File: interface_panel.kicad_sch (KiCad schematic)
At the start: 20 parts, among them J1 Conn_02x04_Odd_Even, J2 but1, J3 but2, J4 but3, J5 Led, U2 ATmega328P-P, Y1 Crystal

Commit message: oled Production
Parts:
- removed J1: Conn_02x04_Odd_Even, Connector_IDC:IDC-Header_2x04_P2.54mm_Vertical, symbol Connector_Generic:Conn_02x04_Odd_Even
- added J6: Conn_01x02_Socket, Connector_PinHeader_1.27mm:PinHeader_1x02_P1.27mm_Vertical, symbol Connector:Conn_01x02_Socket
- added J7: Conn_02x05_Odd_Even, Connector_IDC:IDC-Header_2x05_P2.54mm_Vertical, symbol Connector_Generic:Conn_02x05_Odd_Even
- added R2: 10k, Resistor_THT:R_Axial_DIN0204_L3.6mm_D1.6mm_P5.08mm_Horizontal, symbol Device:R
- H1, H2, H3, H4: footprint (none) -> MountingHole:MountingHole_2.2mm_M2
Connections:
- net 5V: now also U2.20 (AVCC), J7.1 (Pin_1), R2.1
- net BT-1: now also J7.5 (Pin_5)
- net BT-2: now also J7.7 (Pin_7)
- net BT-Pwr: now also J7.3 (Pin_3)
- net GND: now also J6.2 (Pin_2), J7.2 (Pin_2)
- net RX: now also J7.6 (Pin_6)
- net S. LED: now also J7.4 (Pin_4)
- net TX: now also J7.8 (Pin_8)
- net at U2.1 (~{RESET}/PC6): now also J6.1 (Pin_1), R2.2
- net D7: now reaches U2.13 (PD7)
- net D7: now also J7.10 (Pin_10)
- net D11: now reaches U2.17 (PB3)
- net D11: now also J7.9 (Pin_9)

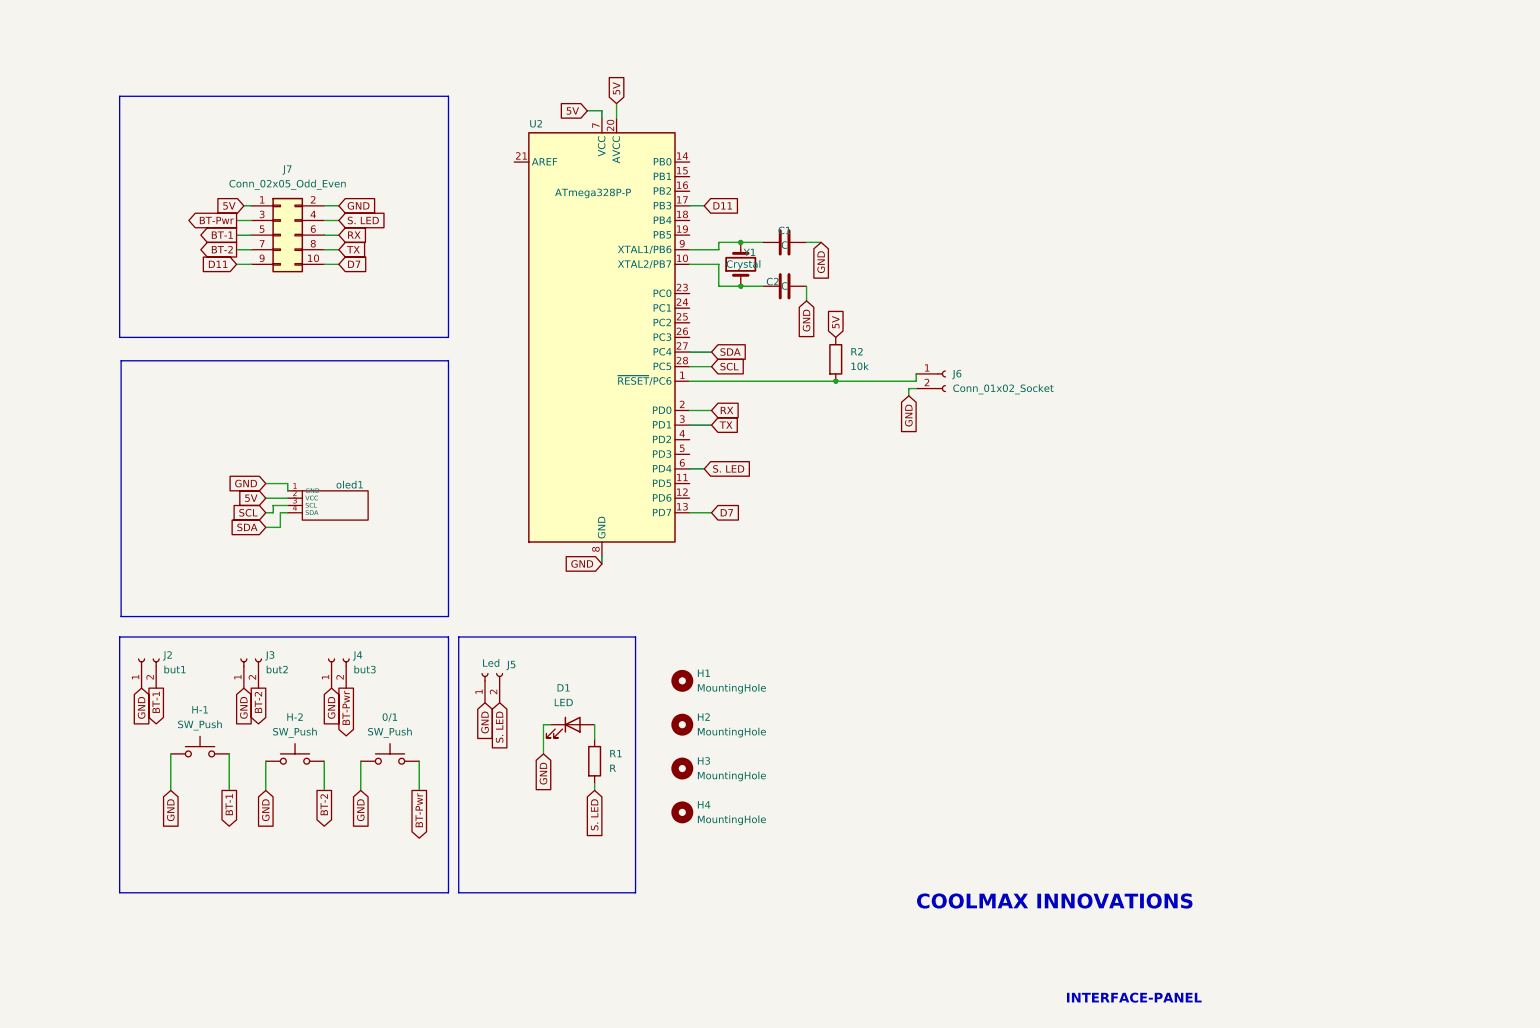
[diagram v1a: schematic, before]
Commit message: 7segment added
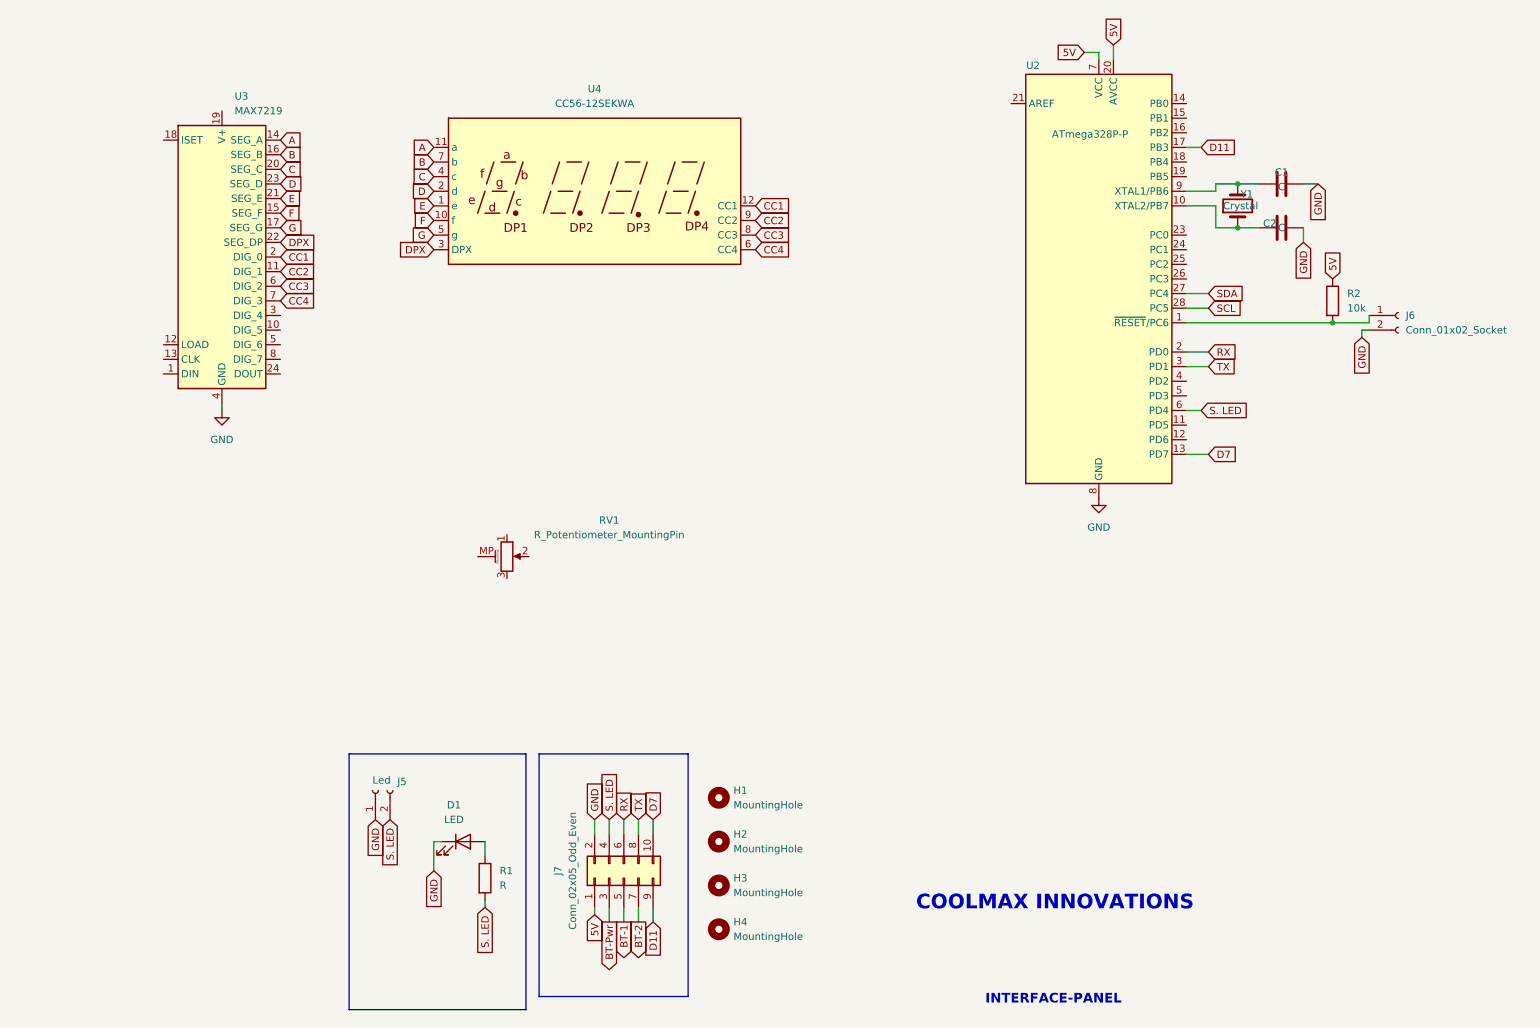
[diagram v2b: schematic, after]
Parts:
- removed 0/1, H-1, H-2: SW_Push, pushbutt_12x12x7.3:SW_TS14-1212-140-BK-160-SCR-D, symbol Switch:SW_Push
- removed J2: but1, Connector_JST:JST_EH_B2B-EH-A_1x02_P2.50mm_Vertical, symbol Connector:Conn_01x02_Socket
- removed J3: but2, Connector_JST:JST_EH_B2B-EH-A_1x02_P2.50mm_Vertical, symbol Connector:Conn_01x02_Socket
- removed J4: but3, Connector_JST:JST_EH_B2B-EH-A_1x02_P2.50mm_Vertical, symbol Connector:Conn_01x02_Socket
- removed U1: ~, symbol New_Library:oled128x32
- removed oled1: ~, oled0.9in:MODULE_DM-OLED096-636, symbol New_Library:oled
- added RV1: R_Potentiometer_MountingPin, Potentiometer_THT:Potentiometer_Alps_RK09K_Single_Horizontal, symbol Device:R_Potentiometer_MountingPin
- added U3: MAX7219, Package_DIP:DIP-24_W7.62mm, symbol Driver_LED:MAX7219
- added U4: CC56-12SEKWA, Display_7Segment:CA56-12SEKWA, symbol Display_Character:CC56-12SEKWA
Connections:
- net GND: now also U3.4 (GND), U3.9 (GND)
- new net A: U3.14 (SEG_A), U4.11 (a)
- new net B: U3.16 (SEG_B), U4.7 (b)
- new net C: U3.20 (SEG_C), U4.4 (c)
- new net CC1: U3.2 (DIG_0), U4.12 (CC1)
- new net CC2: U3.11 (DIG_1), U4.9 (CC2)
- new net CC3: U3.6 (DIG_2), U4.8 (CC3)
- new net CC4: U3.7 (DIG_3), U4.6 (CC4)
- new net D: U3.23 (SEG_D), U4.2 (d)
- new net DPX: U3.22 (SEG_DP), U4.3 (DPX)
- new net E: U3.21 (SEG_E), U4.1 (e)
- new net F: U3.15 (SEG_F), U4.10 (f)
- new net G: U3.17 (SEG_G), U4.5 (g)
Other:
- moved on the sheet: C1, C2, D1, H1, H2, H3, H4, J5, J6, J7, R1, R2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

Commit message: Segment-added
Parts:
- removed RV1: R_Potentiometer_MountingPin, Potentiometer_THT:Potentiometer_Alps_RK09K_Single_Horizontal, symbol Device:R_Potentiometer_MountingPin
- removed U3: MAX7219, Package_DIP:DIP-24_W7.62mm, symbol Driver_LED:MAX7219
- removed U4: CC56-12SEKWA, Display_7Segment:CA56-12SEKWA, symbol Display_Character:CC56-12SEKWA
- added H5, H6, PWR1: SW_Push, Button_Switch_THT:SW_PUSH-12mm, symbol Switch:SW_Push
- added Q1, Q2: BC547, Package_TO_SOT_THT:TO-92_Inline, symbol Transistor_BJT:BC547
- added R10, R11, R12, R3, R4, R5, R6, R7, R8, R9: R, Resistor_THT:R_Axial_DIN0204_L3.6mm_D1.6mm_P5.08mm_Horizontal, symbol Device:R
- added U1, U4: SM420561N, Display_7Segment:7SegmentLED_LTS6760_LTS6780, symbol Display_Character:SM420561N
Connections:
- net A: now also R7.2, U1.7 (A), U4.7 (A)
- net B: now also R8.2, U1.6 (B), U4.6 (B)
- net BT-1: now also H5.1
- net BT-2: now also H6.1
- net BT-Pwr: now also PWR1.1
- net C: now also R9.2, U1.4 (C), U4.4 (C)
- net CC1: now also Q1.2 (B), R3.2
- net CC2: now also Q2.2 (B), R4.2
- net D: now also R10.2, U1.2 (D), U4.2 (D)
- net D7: no longer U2.13 (PD7)
- net DPX: now also R6.2, U1.5 (DP), U4.5 (DP)
- net E: now also R11.2, U1.1 (E), U4.1 (E)
- net F: now also R12.2, U1.9 (F), U4.9 (F)
- net G: now also R5.2, U1.10 (G), U4.10 (G)
- net GND: now also H5.2, H6.2, PWR1.2, Q1.3 (E), Q2.3 (E)
- net S. LED: now also U2.18 (PB4); no longer U2.6 (PD4)
- net at U2.11 (PD5): now also R9.1
- net at U2.12 (PD6): now also R10.1
- net at U2.14 (PB0): now also R12.1
- net at U2.15 (PB1): now also R5.1
- net at U2.16 (PB2): now also R3.1
- net D13: now reaches U2.19 (PB5)
- net D13: now also J7.9 (Pin_9)
- net at U2.4 (PD2): now also R6.1
- net at U2.5 (PD3): now also R7.1
- net D11: no longer names the net of U2.17 (PB3)
- net D11: now also R4.1; no longer J7.9 (Pin_9)
- net SCL: no longer names the net of U2.28 (PC5)
- net SDA: no longer names the net of U2.27 (PC4)
- new net: Q2.1 (C), U4.3 (CC), U4.8 (CC)
- new net: Q1.1 (C), U1.3 (CC), U1.8 (CC)
- new net: R11.1, U2.13 (PD7)
- new net: R8.1, U2.6 (PD4)

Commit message: updated
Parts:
- added J1: B1, Connector_JST:JST_EH_B2B-EH-A_1x02_P2.50mm_Vertical, symbol Connector:Conn_01x02_Socket
- added J2: B2, Connector_JST:JST_EH_B2B-EH-A_1x02_P2.50mm_Vertical, symbol Connector:Conn_01x02_Socket
- added J3: BP, Connector_JST:JST_EH_B2B-EH-A_1x02_P2.50mm_Vertical, symbol Connector:Conn_01x02_Socket
- added JP1: sda, Jumper:SolderJumper-2_P1.3mm_Open_Pad1.0x1.5mm, symbol Jumper:SolderJumper_2_Open
- added JP2: scl, Jumper:SolderJumper-2_P1.3mm_Open_Pad1.0x1.5mm, symbol Jumper:SolderJumper_2_Open
- added R13, R14: R, Resistor_THT:R_Axial_DIN0204_L3.6mm_D1.6mm_P5.08mm_Horizontal, symbol Device:R
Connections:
- net BT-1: now also J1.2 (Pin_2)
- net BT-2: now also J2.2 (Pin_2)
- net BT-Pwr: now also J3.2 (Pin_2)
- net CC1: now also R13.2
- net CC2: now also R14.2
- net GND: now also J1.1 (Pin_1), J2.1 (Pin_1), J3.1 (Pin_1), R13.1, R14.1
- net RX: now also JP1.2 (B)
- net TX: now also JP2.2 (B)
- net at U2.27 (PC4): now also JP1.1 (A)
- net at U2.28 (PC5): now also JP2.1 (A)
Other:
- moved on the sheet: R2

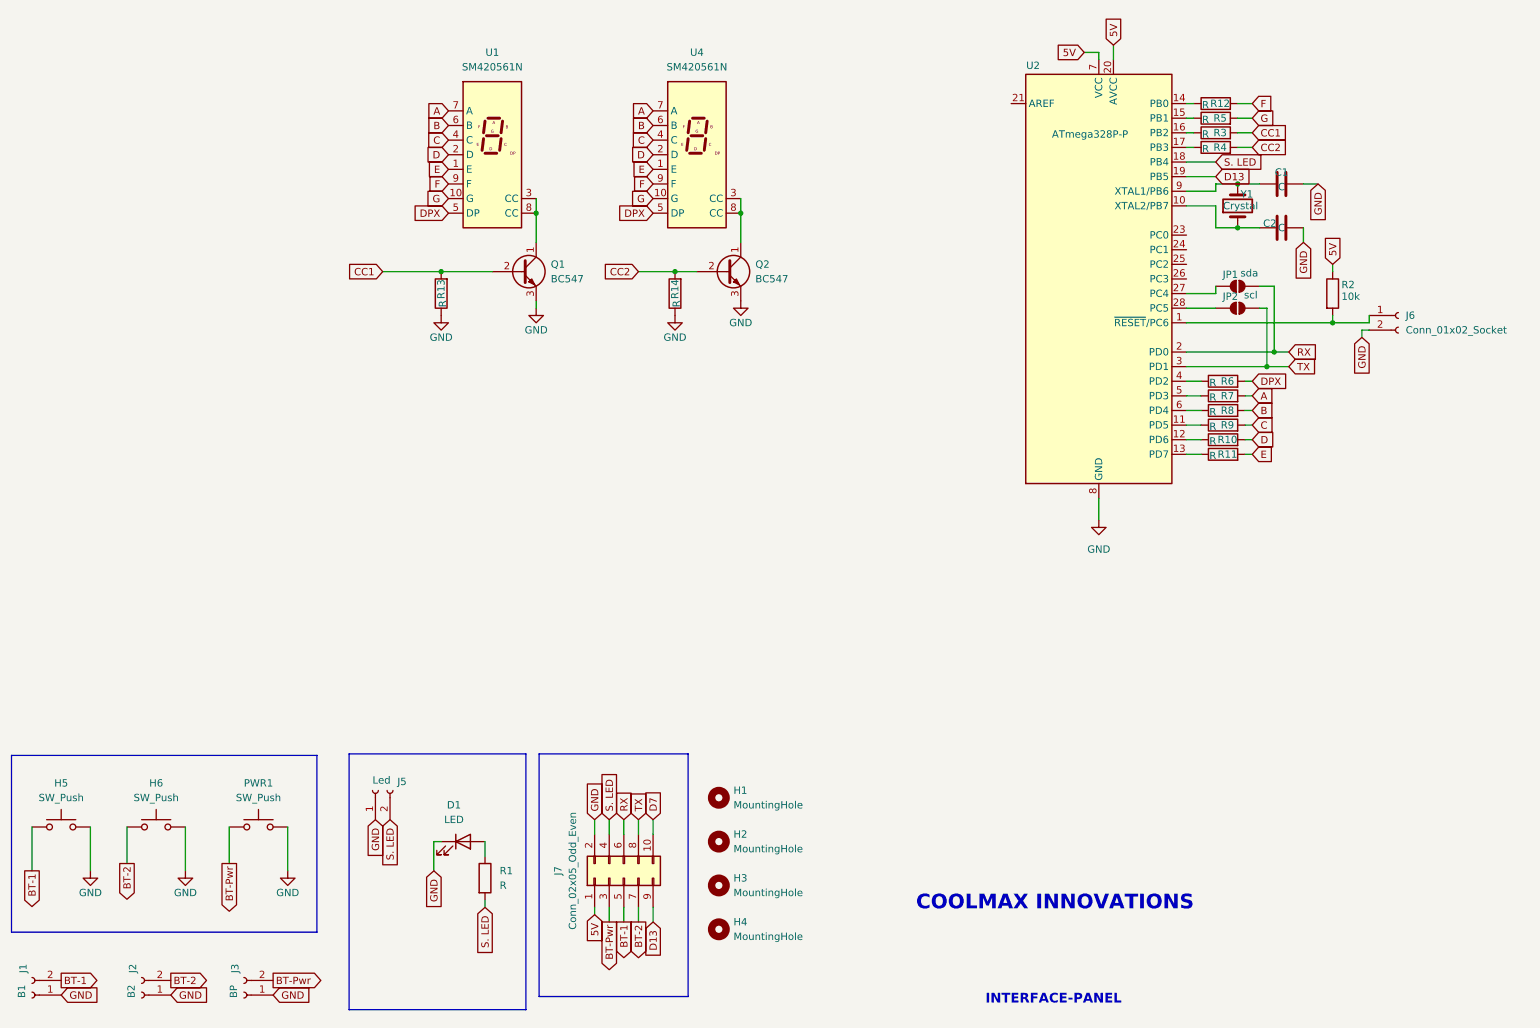
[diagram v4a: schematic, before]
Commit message: new-layout with 7seg and fpc connector
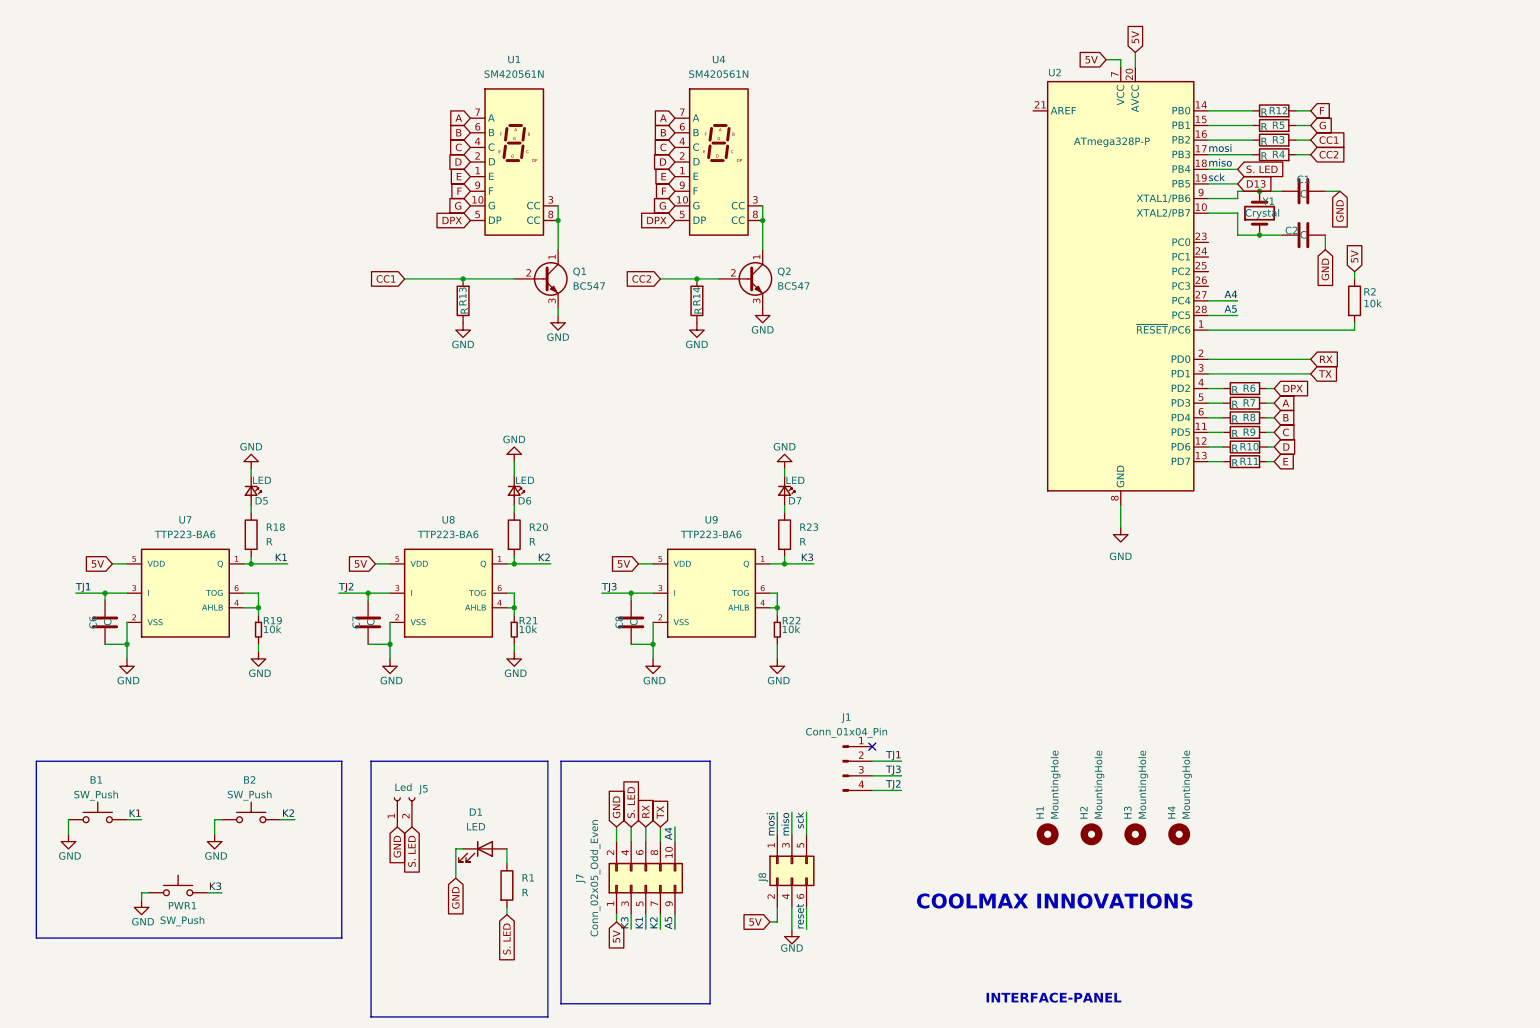
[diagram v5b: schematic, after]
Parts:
- removed H5, H6: SW_Push, Button_Switch_THT:SW_PUSH-12mm, symbol Switch:SW_Push
- removed J1: B1, Connector_JST:JST_EH_B2B-EH-A_1x02_P2.50mm_Vertical, symbol Connector:Conn_01x02_Socket
- removed J2: B2, Connector_JST:JST_EH_B2B-EH-A_1x02_P2.50mm_Vertical, symbol Connector:Conn_01x02_Socket
- removed J3: BP, Connector_JST:JST_EH_B2B-EH-A_1x02_P2.50mm_Vertical, symbol Connector:Conn_01x02_Socket
- removed J6: Conn_01x02_Socket, Connector_PinHeader_1.27mm:PinHeader_1x02_P1.27mm_Vertical, symbol Connector:Conn_01x02_Socket
- removed JP1: sda, Jumper:SolderJumper-2_P1.3mm_Open_Pad1.0x1.5mm, symbol Jumper:SolderJumper_2_Open
- removed JP2: scl, Jumper:SolderJumper-2_P1.3mm_Open_Pad1.0x1.5mm, symbol Jumper:SolderJumper_2_Open
- added B1, B2: SW_Push, Button_Switch_THT:SW_PUSH-12mm, symbol Switch:SW_Push
- added C6, C7, C8: C, Capacitor_SMD:C_1206_3216Metric_Pad1.33x1.80mm_HandSolder, symbol Device:C
- added D5, D6, D7: LED, PCM_SparkFun-LED:LED_1206_3216Metric, symbol PCM_SparkFun-LED:LED
- added J1: Conn_01x04_Pin, Connector_FFC-FPC:Amphenol_F32Q-1A7x1-11004_1x04-1MP_P0.5mm_Horizontal, symbol Connector:Conn_01x04_Pin
- added J8: `, Connector_PinHeader_2.54mm:PinHeader_2x03_P2.54mm_Vertical, symbol Connector_Generic:Conn_02x03_Odd_Even
- added R18, R20, R23: R, Resistor_SMD:R_1206_3216Metric_Pad1.30x1.75mm_HandSolder, symbol Device:R
- added R19, R21, R22: 10k, Resistor_SMD:R_1206_3216Metric_Pad1.30x1.75mm_HandSolder, symbol Device:R
- added U7, U8, U9: TTP223-BA6, TTP223-BA6:SOT23-6, symbol TTP223:TTP223-BA6
- C1, C2: footprint Capacitor_THT:C_Disc_D3.0mm_W1.6mm_P2.50mm -> Capacitor_SMD:C_1206_3216Metric_Pad1.33x1.80mm_HandSolder
- D1: footprint LED_THT:LED_D3.0mm -> PCM_SparkFun-LED:LED_1206_3216Metric
- R1, R10, R11, R12, R13, R14, R2, R3, R4, R5, R6, R7, R8, R9: footprint Resistor_THT:R_Axial_DIN0204_L3.6mm_D1.6mm_P5.08mm_Horizontal -> Resistor_SMD:R_1206_3216Metric_Pad1.30x1.75mm_HandSolder
- U2: footprint Package_DIP:DIP-28_W7.62mm -> atmega328p-smd:QFP80P900X900X120-32N
- Y1: footprint Crystal:Crystal_HC18-U_Vertical -> Crystal:Crystal_SMD_HC49-SD
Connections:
- net D7 is gone; now on net A4: J7.10 (Pin_10)
- net 5V: now also J8.2 (Pin_2), U7.5 (VDD), U8.5 (VDD), U9.5 (VDD)
- net D13: now also J8.5 (Pin_5); no longer J7.9 (Pin_9)
- net GND: now also PWR1.1, B1.1, B2.1, C6.1, C7.1, C8.1, D5.1 (K), D6.1 (K), D7.1 (K), J8.4 (Pin_4), R19.2, R21.2, R22.2, U7.2 (VSS), U8.2 (VSS), U9.2 (VSS); no longer PWR1.2
- net S. LED: now also J8.3 (Pin_3)
- net A5: now reaches U2.28 (PC5)
- net A5: now also J7.9 (Pin_9)
- net A4: now reaches U2.27 (PC4)
- net mosi: now reaches R4.1, U2.17 (PB3)
- net mosi: now also J8.1 (Pin_1)
- net BT-1 renamed K1
- net K1: now also B1.2, R18.2, U7.1 (Q)
- net BT-2 renamed K2
- net K2: now also B2.2, R20.2, U8.1 (Q)
- net BT-Pwr renamed K3
- net K3: now also PWR1.2, R23.2, U9.1 (Q); no longer PWR1.1
- new net: R22.1, U9.4 (AHLB), U9.6 (TOG)
- new net: R21.1, U8.4 (AHLB), U8.6 (TOG)
- new net: D6.2 (A), R20.1
- new net: R19.1, U7.4 (AHLB), U7.6 (TOG)
- new net: D7.2 (A), R23.1
- new net: D5.2 (A), R18.1
- new net TJ1: C6.2, J1.2 (Pin_2), U7.3 (I)
- new net TJ2: C7.2, J1.4 (Pin_4), U8.3 (I)
- new net TJ3: C8.2, J1.3 (Pin_3), U9.3 (I)
- new net reset: J8.6 (Pin_6)
- no-connect marks 0 -> 1
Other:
- moved on the sheet: C1, C2, D1, H1, H2, H3, H4, J5, J7, Q1, Q2, R1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
